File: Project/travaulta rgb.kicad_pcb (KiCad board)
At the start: 4 copper layers, 208.3 x 75.8 mm, 107 parts, among them J1 ARGB, SW1 EC_SW, SW10 EC_SW, SW11 EC_SW, SW12 EC_SW, SW13 EC_SW, SW14 EC_SW, SW15 EC_SW, SW16 EC_SW, SW17 EC_SW, SW18 EC_SW, SW19 EC_SW, SW2 EC_SW, SW20 EC_SW, SW21 EC_SW, SW22 EC_SW, SW23 EC_SW, SW24 EC_SW, SW25 EC_SW, SW26 EC_SW, SW27 EC_SW, SW28 EC_SW, SW29 EC_SW, SW3 EC_SW, SW30 EC_SW, SW31 EC_SW, SW32 EC_SW, SW33 EC_SW, SW34 EC_SW, SW35 EC_SW, SW36 EC_SW, SW37 EC_SW, SW38 BOOT0, SW4 EC_SW, SW5 EC_SW, SW6 EC_SW, SW7 EC_SW, SW8 EC_SW, SW9 EC_SW, U1 STM32F401CBUx, U2 XC6206PxxxMR, U3 74HC4051, U4 74HC4051, U5 OPA350, Y1 8 MHz

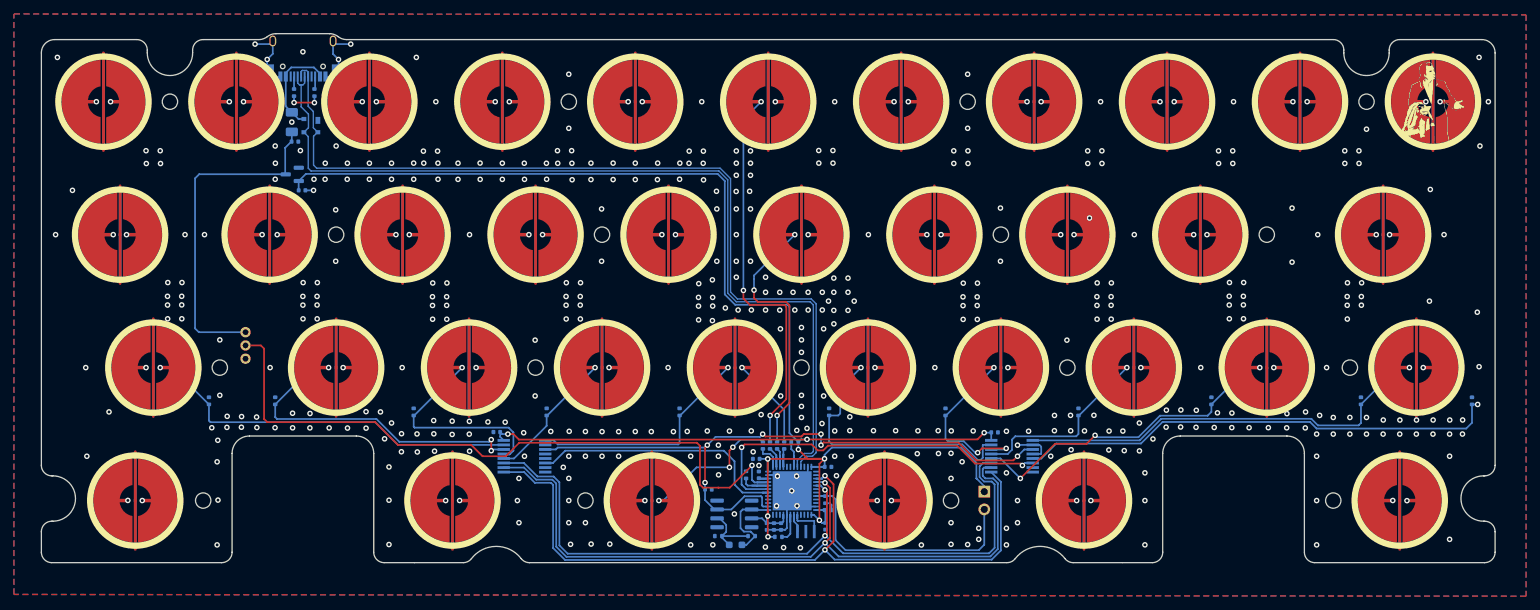
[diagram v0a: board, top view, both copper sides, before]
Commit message: added rgb breakout to HHKB&WKL
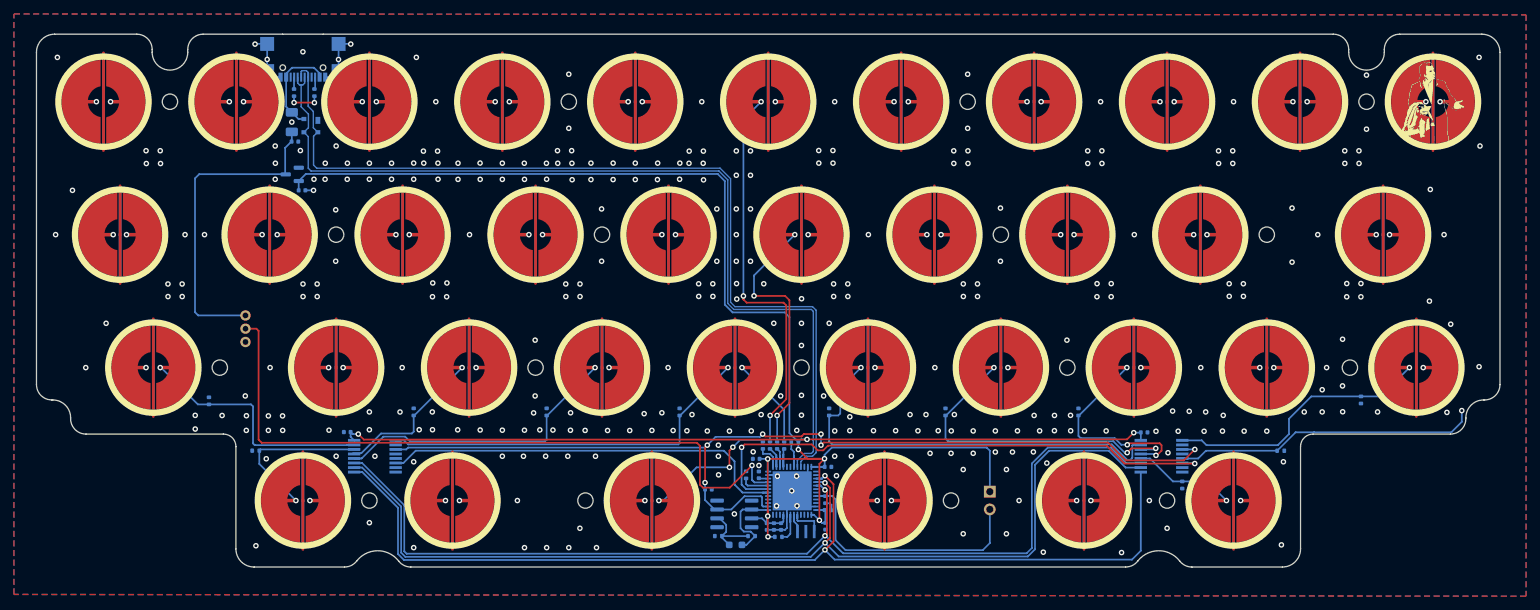
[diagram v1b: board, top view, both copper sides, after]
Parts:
- J1: footprint cipulot_parts:PinHeader_RGB strip -> Connector_PinHeader_1.27mm:PinHeader_1x03_P1.27mm_Vertical
- USB1: footprint cipulot_parts:XUNPU-TYPEC-312DSS-ACP16-Assembly -> cipulot_parts:TYPEC-304YSSW-ACP16
- moved R5 28.3 mm to (222.7, 107.2), turned to 0 degrees
- moved SW32 24.0 mm to (82.5, 114.3), turned to 180 degrees
- moved H14 23.8 mm to (92.1, 114.3)
- moved H17 23.8 mm to (206.4, 114.3)
- moved SW37 23.8 mm to (215.9, 114.3)
- moved C12 21.4 mm to (203.1, 104.5)
- moved U3 21.4 mm to (205.6, 108.0)
- moved C13 21.4 mm to (88.9, 104.5)
- moved U4 21.4 mm to (92.9, 108.0)
- moved R14 12.8 mm to (208.5, 112.1), turned to -90 degrees
- moved R13 7.67 mm to (75.8, 107.2), turned to 180 degrees
- moved G*** 5.56 mm to (250.8, 76.2)
- moved J1 2.40 mm to (74.3, 90.9)
- moved G*** 0.87 mm to (197.7, 72.8)
- moved SW38 0.79 mm to (181.0, 113.0)
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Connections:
- SW32 pad 2: COL0 -> COL1
- SW37 pad 2: COL9 -> COL8
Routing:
- net ROW3: track 340.7 -> 221.9 mm
- net APLEX_OUT_PIN_0: track 94.2 -> 140.6 mm
- net VBAT: track 272.7 -> 318.1 mm
- net COL9: track 127.3 -> 85.8 mm, vias 4 -> 3
- net COL0: track 122.3 -> 81.4 mm, vias 4 -> 3
- net AMUX_SEL_1: track 109.4 -> 149.5 mm
- net AMUX_SEL_0: track 107.5 -> 147.3 mm
- net AMUX_SEL_2: track 109.2 -> 148.7 mm
- net APLEX_EN_PIN_1: track 53.2 -> 78.0 mm
- net COL10: track 114.7 -> 89.9 mm
- net COL3: track 91.8 -> 115.0 mm
- net COL5: track 107.3 -> 128.8 mm
- net COL6: track 70.9 -> 92.3 mm
- net COL4: track 79.1 -> 100.5 mm
- net APLEX_EN_PIN_0: track 37.9 -> 59.3 mm
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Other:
- board size 208.3 x 75.8 mm -> 209.7 x 76.4 mm
- board text removed: "WKL"
